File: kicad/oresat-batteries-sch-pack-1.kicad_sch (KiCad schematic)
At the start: 85 parts, among them Q10 SI7111EDN-T1-GE3, Q12 SI7111EDN-T1-GE3, Q13 SI7111EDN-T1-GE3, Q14 NTR4101, Q15 NTR4101, Q16 SI7111EDN-T1-GE3, Q17 SI7111EDN-T1-GE3, Q18 SI7111EDN-T1-GE3, Q19 SI7111EDN-T1-GE3, Q29 SQS484ENW-T1_GE3, Q6 PMV45ENR, Q7 PMV45ENR, Q8 PMV45ENR, Q9 PMV45ENR, U10 LTC4412, U11 LTC4412, U12 MAX17205G, U8 S-8209AAA-T8T1U, U9 S-8209AAA-T8T1U

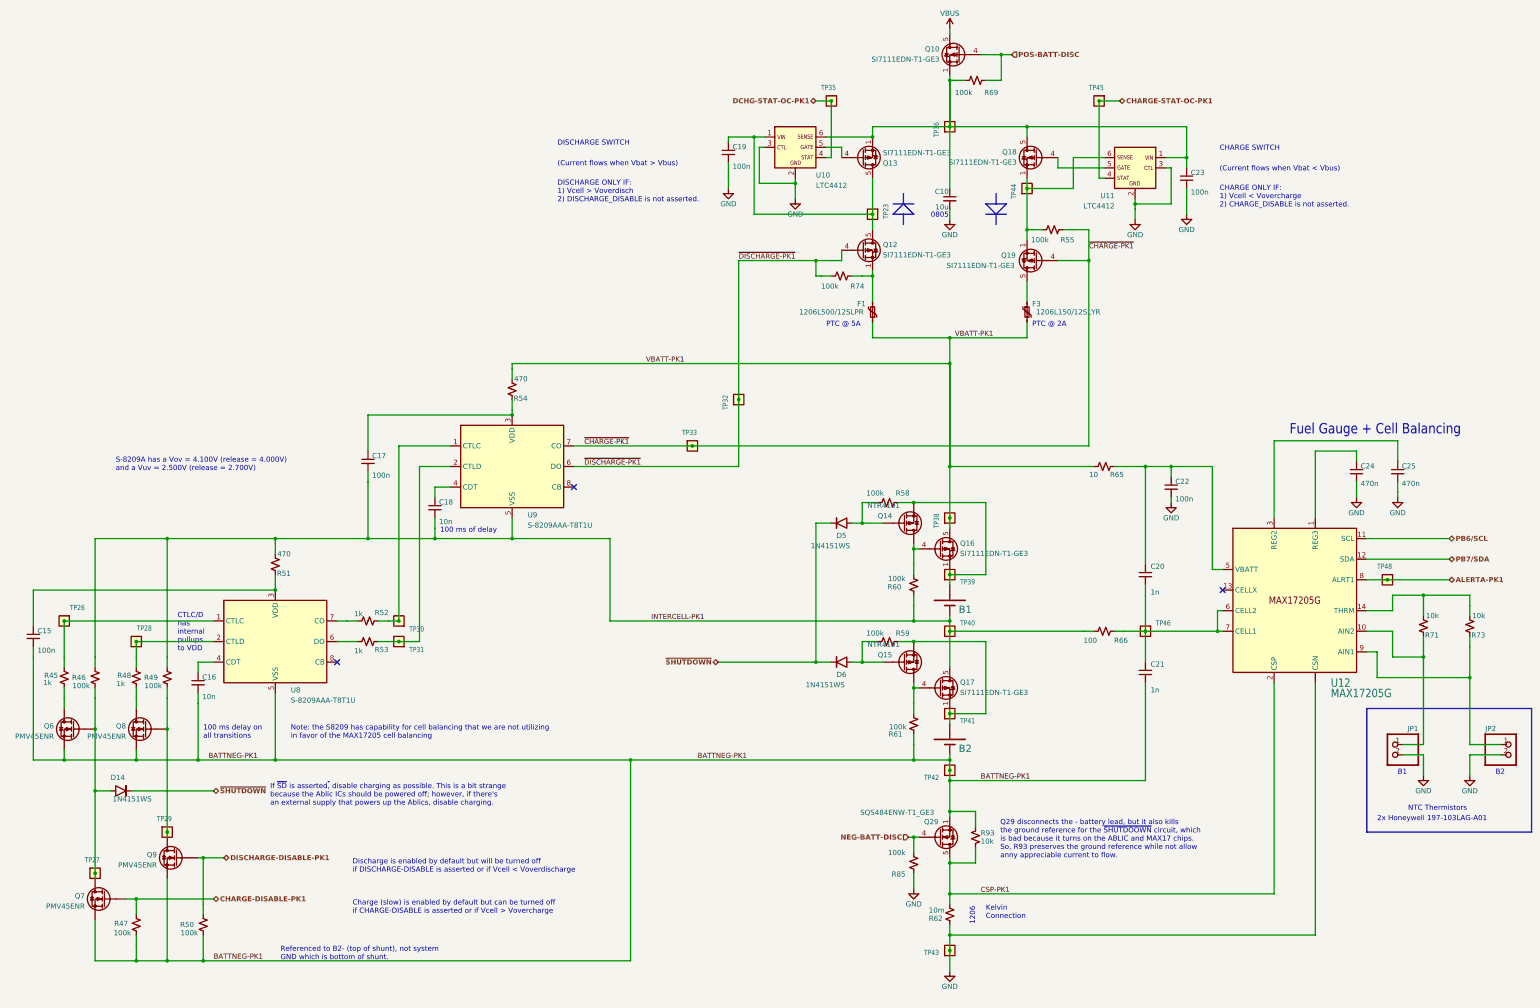
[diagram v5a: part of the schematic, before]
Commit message: Updated BOM, ready for polish and switch to MCXN
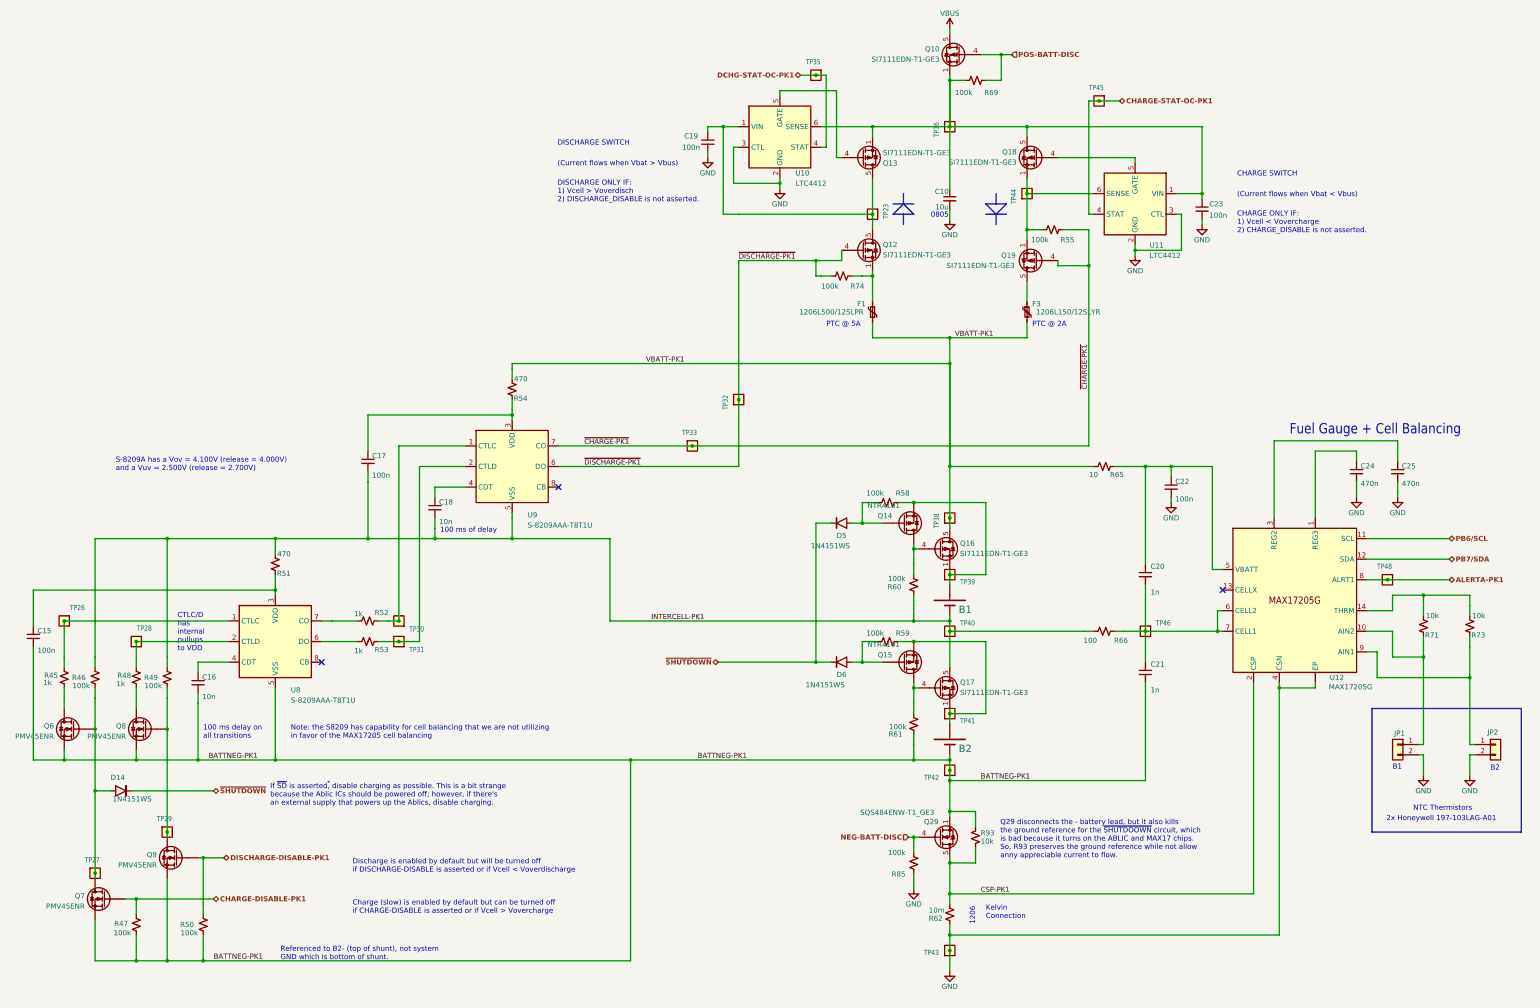
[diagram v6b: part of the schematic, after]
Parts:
- B1, B2: footprint oresat-batteries:18650 -> oresat-misc:18650
- JP1, JP2: footprint oresat-batteries:1X02 -> Connector_PinHeader_2.54mm:PinHeader_1x02_P2.54mm_Vertical; symbol oresat-batteries-eagle-import:PINHD-1X2 -> Connector_Generic:Conn_01x02
- U10, U11: footprint oresat-batteries:SOT23-6 -> Package_TO_SOT_SMD:TSOT-23-6; symbol oresat-batteries-eagle-import:LTC4412 -> Power_Management:LTC4412xS6
- U12: footprint oresat-batteries:21-0137I_T1433-2 -> Package_DFN_QFN:TDFN-14-1EP_3x3mm_P0.4mm_EP1.78x2.35mm_ThermalVias; symbol oresat-batteries-eagle-import:MAX17205G -> oresat-ics:MAX17205G; DIS Distributor -> DigiKey; MFR Maxim -> Analog Devices
- U8, U9: footprint oresat-batteries:TSSOP8 -> Package_SO:TSSOP-8_4.4x3mm_P0.65mm; symbol oresat-batteries-eagle-import:S-8209AXXT -> oresat-ics:S-8209AXXT
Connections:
- net GND: now also U12.15 (EP); no longer U12.EP (CSN)
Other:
- moved on the sheet: C19, C23, TP35, TP44, U10, U11

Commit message: Not sure what changed from back in February, but committing anyway :)
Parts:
- added RT1, RT2: 10k NTC TH, symbol Device:Thermistor
- C10: DIS Digi-Key -> DigiKey; DPN 1276-2893-1-ND -> 490-GRT21BC71E106KE13KCT-ND; MFR Samsung -> Murata Electronics; MPN CL21A106KOFNNNE -> GRT21BC71E106KE13K
- C15, C17, C19, C22, C23: DIS Digi-Key -> DigiKey; DPN 399-1099-1-ND -> 399-6856-1-ND; MFR Kemet -> KEMET; MPN C0603C104M4RACTU -> C0603C104K5RACAUTO
- C16, C18: DIS Digi-Key -> DigiKey; DPN 399-7842-1-ND -> 399-12983-1-ND; MFR Kemet -> KEMET; MPN C0603C103M5RACTU -> C0603C103J5RACAUTO
- C20, C21: DIS Digi-Key -> DigiKey; DPN 311-1080-1-ND -> 399-12989-1-ND; MFR Yageo -> KEMET; MPN CC0603KRX7R9BB102 -> C0603C102J5RACAUTO
- C24, C25: DIS Digi-Key -> DigiKey; DPN 399-7934-1-ND -> 399-6820-1-ND; MFR Kemet -> KEMET; MPN C0603C474K4PACTU -> C0603C473K5RACAUTO
- D14, D5, D6: DIS (none) -> DigiKey; DPN (none) -> 112-1N4151WS-E3-08CT-ND; MFR (none) -> Vishay; MPN (none) -> 1N4151WS-E3-08
- F1: DIS (none) -> DigiKey; DPN (none) -> 18-1206L500/12SLPRCT-ND; MFR (none) -> Littelfuse Inc; MPN (none) -> 18-1206L500/12SLPRCT-ND
- F3: DIS (none) -> DigiKey; DPN (none) -> F5765CT-ND; MFR (none) -> Littelfuse Inc; MPN (none) -> F5765CT-ND
- JP1, JP2: DIS (none) -> N/A; DPN (none) -> N/A; MFR (none) -> N/A; MPN (none) -> N/A; now left out of the parts list
- Q10, Q12, Q13, Q16, Q17, Q18, Q19: DPN SI7625DN-T1-GE3CT-ND -> SI7111EDN-T1-GE3CT-ND; MPN SI7625DN-T1-GE3 -> SI7111EDN-T1-GE3
- Q29: DPN (none) -> SQS484ENW-T1_GE3CT-ND; MFR (none) -> Vishay; MPN (none) -> SQS484ENW-T1_GE3
- R45, R48, R52, R53: DIS Yageo -> DigiKey; DPN RC0603JR-071KL -> RMCF0603FT2K70CT-ND; MFR (none) -> Stackpole Electronics; MPN 311-1.0KGRCT-ND -> RMCF0603FT1K00
- R46, R49, R58, R59, R60, R61, R85: DIS Digi-Key -> DigiKey; DPN 311-1.00MHRCT-ND -> RMCF0603FT100KCT-ND; MFR Yageo -> Stackpole Electronics; MPN RC0603FR-071ML -> RMCF0603FT100K
- R47, R50: DIS Digi-Key -> DigiKey; DPN 311-10.0KHRCT-ND -> RMCF0603FT100KCT-ND; MFR Yageo -> Stackpole Electronics; MPN RC0603FR-0710KL -> RMCF0603FT100K
- R51, R54: DIS Digi-Key -> DigiKey; DPN 311-470GRCT-ND -> RMCF0603FT470RCT-ND; MFR Yageo -> Stackpole Electronics; MPN RC0603JR-07470RL -> RMCF0603FT470R
- R55, R69, R74: DIS Digi-Key -> DigiKey; DPN RR08P100KDCT-ND -> RMCF0603FT100KCT-ND; MFR Susumu -> Stackpole Electronics; MPN RR0816P-104-D -> RMCF0603FT100K
- R62: DIS Digi-Key -> DigiKey
- R65: DPN 311-10.0HRCT-ND -> RMCF0603FT10R0CT-ND; MFR Yageo -> Stackpole Electronics; MPN RC0603FR-0710RL -> RMCF0603FT10R0
- R66: DPN 311-100HRCT-ND -> RMCF0603FT100RCT-ND; MFR Yageo -> Stackpole Electronics; MPN RC0603FR-07100RL -> RMCF0603FT100R
- R71, R73: DIS Digi-Key -> DigiKey; DPN 311-10.0KHRCT-ND -> RMCF0603FT10K0CT-ND; MFR Yageo -> Stackpole Electronics; MPN RC0603FR-0710KL -> RMCF0603FT10K0
- R93: DIS Digi-Key -> DigiKey; DPN RR08P4.7KDCT-ND -> RMCF0603FT10K0CT-ND; MFR TE Connectivity -> Stackpole Electronics; MPN RR0816P-472-D -> RMCF0603FT10K0
- U10, U11: DIS Digi-Key -> DigiKey; DPN LTC4412ES6#TRPBFCT-ND -> MAX4211FETE+-ND; MPN LTC4412ES6#TRPBF -> MAX4211FETE
- U12: MPN MAX17205G+T -> MAX17205G
- U8, U9: DIS (none) -> Mouser; DPN (none) -> 628-S-8209AAA-T8T1U
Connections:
- no-connect marks 3 -> 7

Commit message: Updated data, spiffed up the root page, renamed some STM specific OPD signals, synced SCH and BRD, fixed a bunch of DRC errors, NOW ready for MCXN import that will screw everything up.
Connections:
- net PB6/SCL renamed I2C1_SCL
- net PB7/SDA renamed I2C1_SDA
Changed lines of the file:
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@@
 	(title_block
 		(title "OreSat Battery Card")
-		(date "2026-01-10")
+		(date "2026-03-23")
 		(rev "4.0")
 		(company "Portland State Aerospace Society")
@@
 	(wire
 		(pts
-			(xy 278.13 60.96) (xy 278.13 59.69)
-		)
-		(stroke
-			(width 0)
-			(type default)
-		)
-	)
-	(wire
-		(pts
 			(xy 73.66 176.53) (xy 73.66 179.07)
 		)
@@
 		)
 	)
-	(hierarchical_label "PB7{slash}SDA"
+	(hierarchical_label "I2C1_SDA"
 		(shape bidirectional)
 		(at 382.27 151.13 0)
@@
 		)
 	)
-	(hierarchical_label "PB6{slash}SCL"
+	(hierarchical_label "I2C1_SCL"
 		(shape bidirectional)
 		(at 382.27 146.05 0)
@@
 		)
 		(instances
-			(project ""
+			(project "oresat-batteries"
 				(path "/d5070776-2522-4f7b-9d31-10770161e48a/80ae2c22-7932-4cbd-bc9c-a350bdf6c1aa"
 					(reference "Q29")
@@
 		)
 		(instances
-			(project ""
+			(project "oresat-batteries"
 				(path "/d5070776-2522-4f7b-9d31-10770161e48a/80ae2c22-7932-4cbd-bc9c-a350bdf6c1aa"
 					(reference "#PWR041")
